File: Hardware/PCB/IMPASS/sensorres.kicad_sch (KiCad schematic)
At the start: 31 parts, among them J13 SENSORES, U12 MPU-6050, U2 ACS712xLCTR-30A, U3 ACS712xLCTR-30A, U4 ACS712xLCTR-30A, U5 ACS712xLCTR-30A, U6 ACS712xLCTR-30A, U7 ACS712xLCTR-30A, U8 LM75B, U9 AS5047D

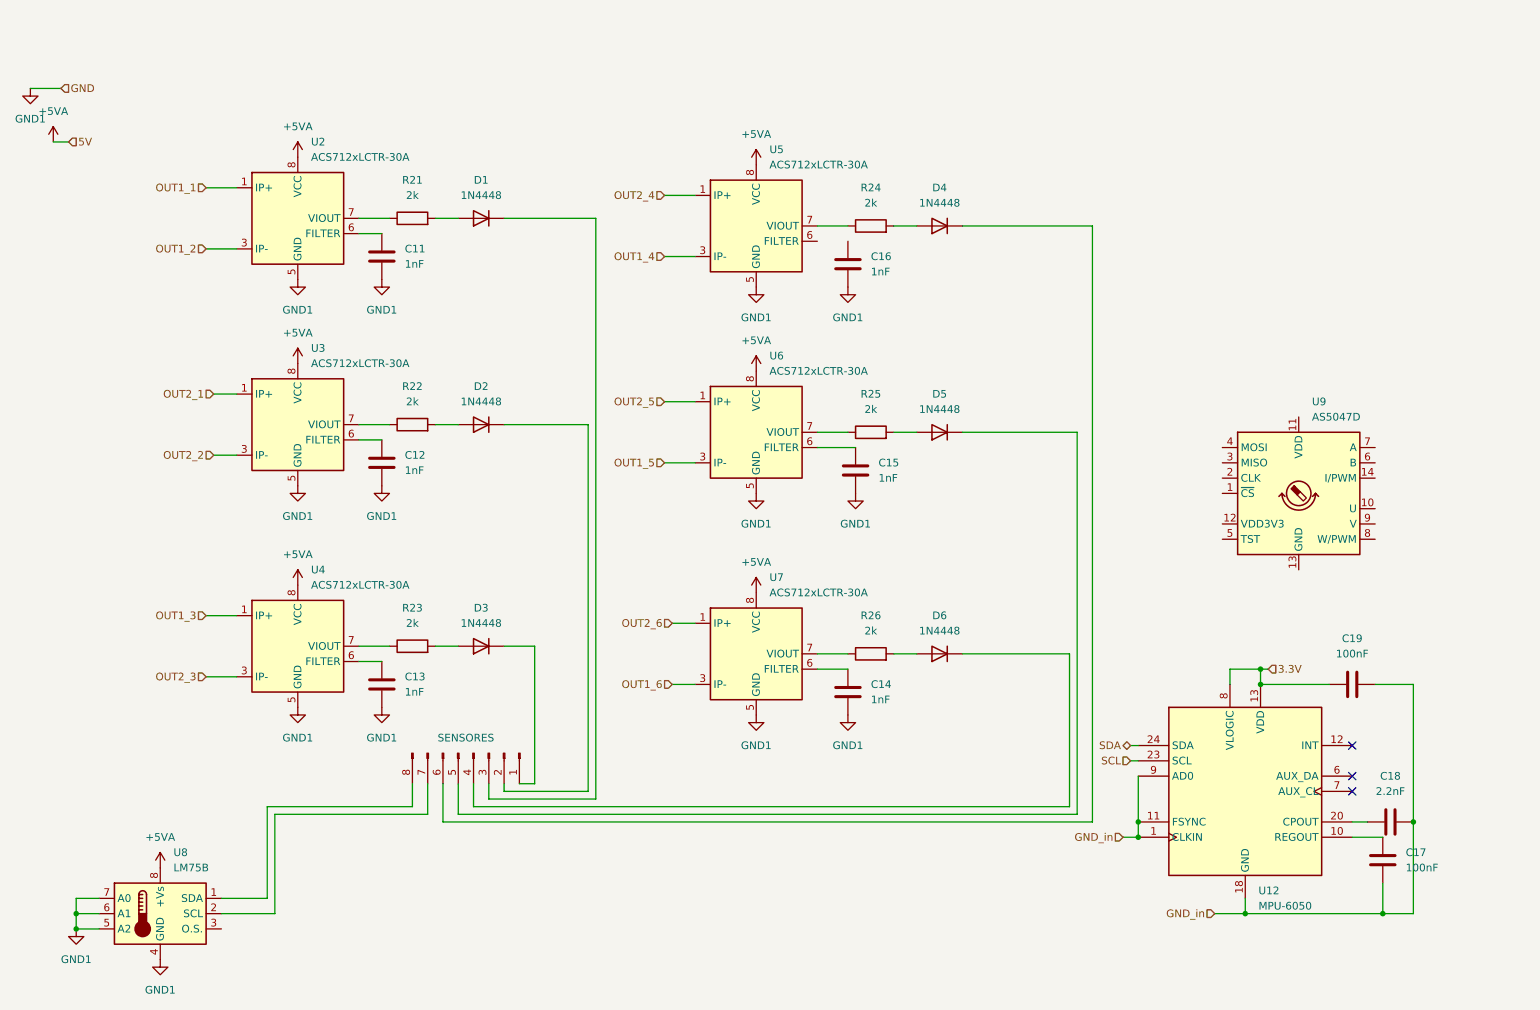
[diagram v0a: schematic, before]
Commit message: Restore all the schematics
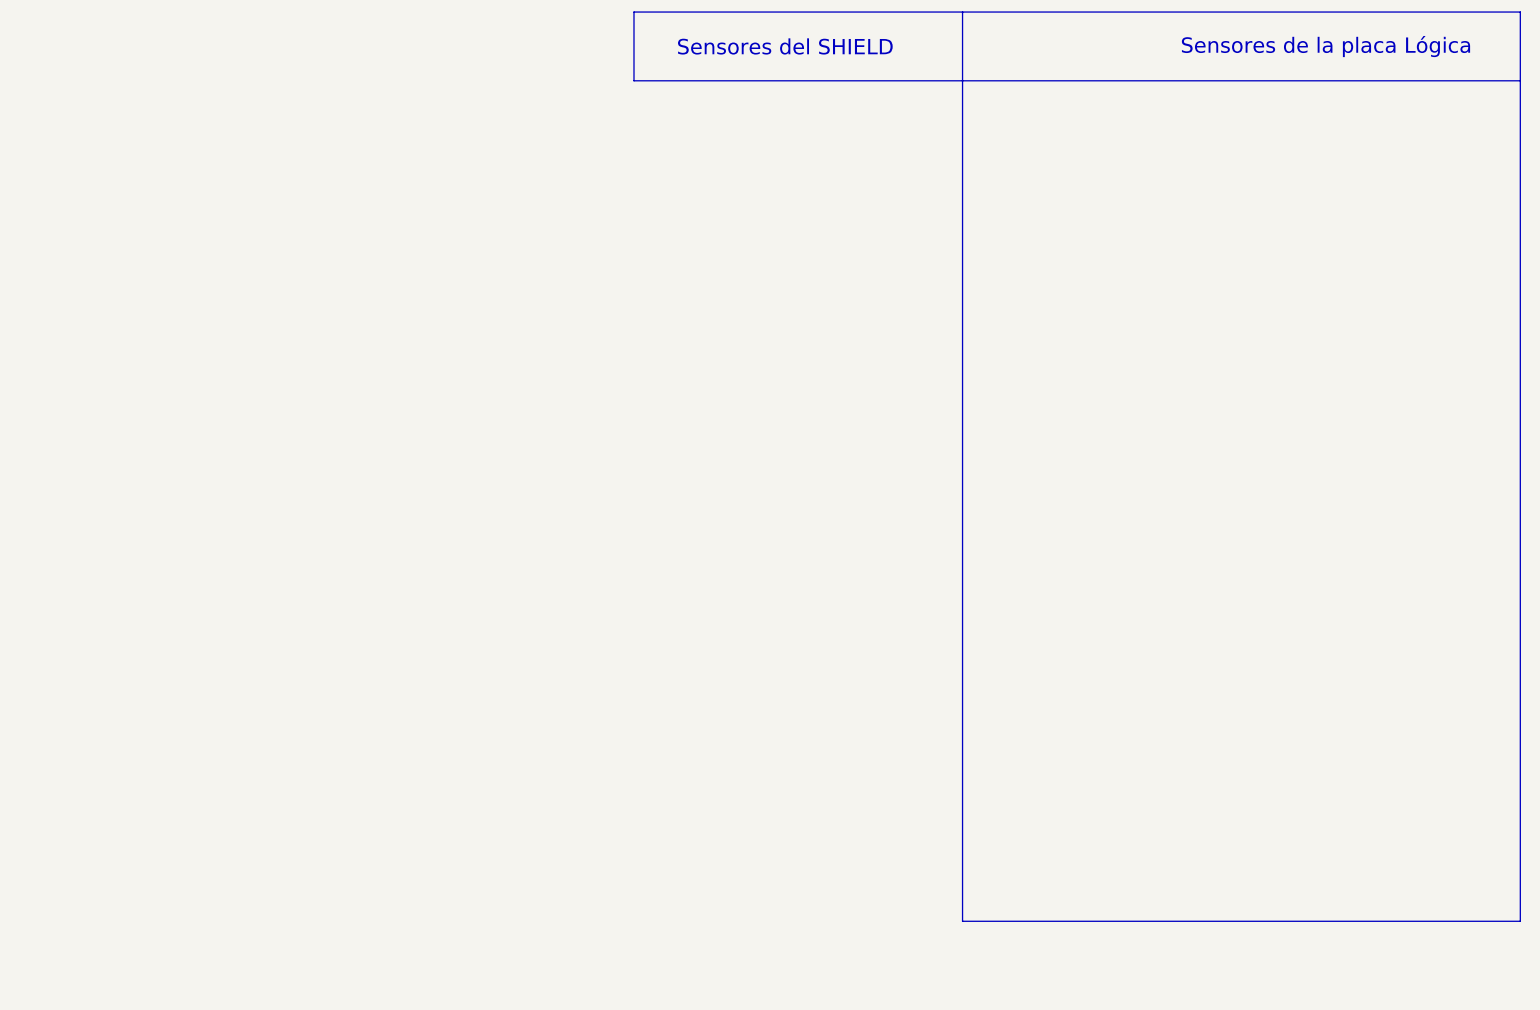
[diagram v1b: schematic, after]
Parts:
- removed C11, C12, C13, C14, C15, C16: 1nF, Capacitor_SMD:C_0603_1608Metric, symbol Device:C
- removed C17, C19: 100nF, Capacitor_SMD:C_0603_1608Metric, symbol Device:C
- removed C18: 2.2nF, Capacitor_SMD:C_0603_1608Metric, symbol Device:C
- removed D1, D2, D3, D4, D5, D6: 1N4448, Diode_THT:D_DO-35_SOD27_P2.54mm_Vertical_AnodeUp, symbol Diode:1N4448
- removed J13: SENSORES, Connector_PinHeader_2.54mm:PinHeader_1x08_P2.54mm_Vertical, symbol Connector:Conn_01x08_Pin
- removed R21, R22, R23, R24, R25, R26: 2k, Resistor_SMD:R_0603_1608Metric, symbol Device:R
- removed U12: MPU-6050, Sensor_Motion:InvenSense_QFN-24_4x4mm_P0.5mm, symbol Sensor_Motion:MPU-6050
- removed U2, U3, U4, U5, U6, U7: ACS712xLCTR-30A, Package_SO:SOIC-8_3.9x4.9mm_P1.27mm, symbol Sensor_Current:ACS712xLCTR-30A
- removed U8: LM75B, Package_SO:SOIC-8_3.9x4.9mm_P1.27mm, symbol Sensor_Temperature:LM75B
- removed U9: AS5047D, Package_SO:TSSOP-14_4.4x5mm_P0.65mm, symbol Sensor_Magnetic:AS5047D
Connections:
- no-connect marks 3 -> 0
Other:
- note added: "Sensores de la placa Lógica"
- note added: "Sensores del SHIELD"
- company: (none) -> Luis Miguel Carmona Cortés
- title: (none) -> IMPASS 
